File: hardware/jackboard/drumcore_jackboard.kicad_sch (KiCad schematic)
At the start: 11 parts, among them J1 PAD1_TRS_6.35MM, J2 PAD2_TRS_6.35MM, J3 PAD3_TRS_6.35MM, J4 PAD4_TRS_6.35MM, J5 PAD5_TRS_6.35MM, J6 PAD6_TRS_6.35MM, J7 PAD7_TRS_6.35MM, J8 PAD8_TRS_6.35MM, J9 LINK_TO_MAINBOARD, U1 HC4067_CHANNELS, U2 HC4067_CTRL

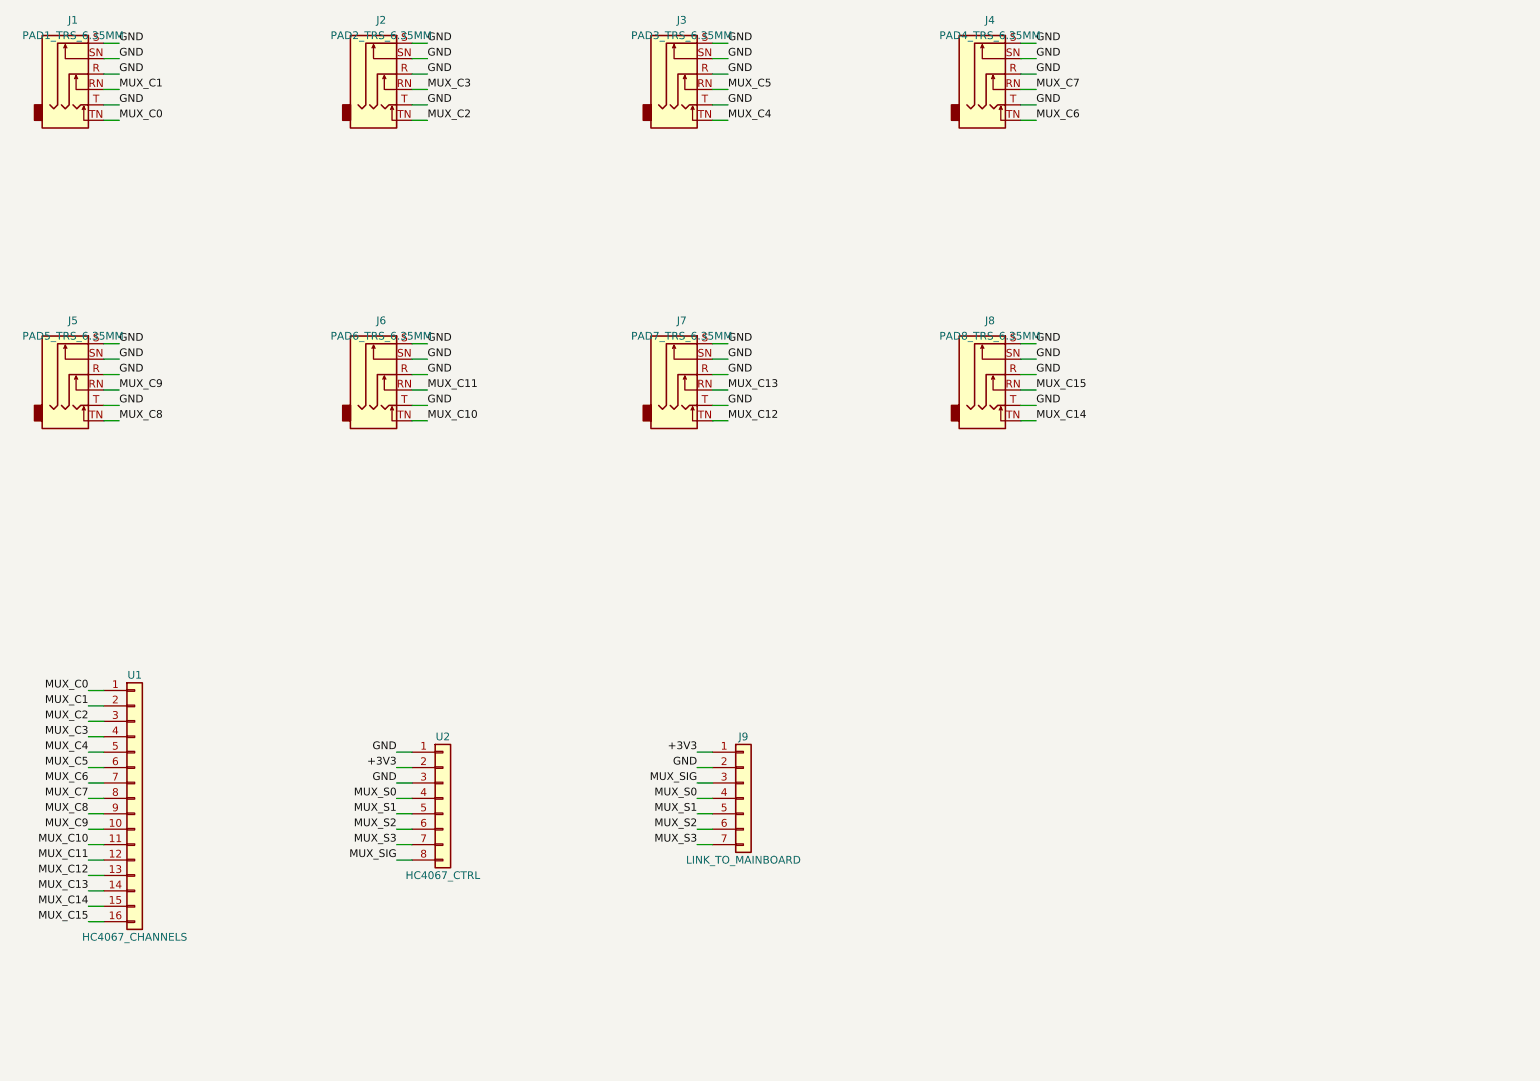
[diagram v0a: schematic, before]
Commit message: Jackboard: pinos T/R corrigidos + rede de protecao por canal; teste do sensor hall
Hardware (hardware/jackboard):
- Esquematico: jacks usavam TN/RN (contato normal/switched) como sinal por
  engano - corrigido pra usar T/R de verdade (Tip=par, Ring=impar), com
  TN/RN/S/SN todos em GND.
- Adicionada rede de protecao por canal (16x): resistor serie 100R + resistor
  paralelo 100k + diodo BAT85, mesma topologia do esquema de referencia da
  HelloDrum-arduino-Library pro MUX (docs/circuit.md).
- PCB: jacks recriados com a netlist corrigida (sync limpo, sem conflito de
  net reatribuido em pad ja roteado) e realinhados no passo fisico de
  22.5mm; os 48 componentes de protecao posicionados no espaco livre entre
  as duas colunas de pads de cada jack; cluster do mux (U1/U2) e do header
  de link (J9) recentralizado sobre a fileira de jacks.

Firmware:
- main.cpp: teste direto do sensor hall (SS49E) do controlador de HH agora
  le so' o GPIO17 (Pad 1 como PAD_SINGLE) - antes lia GPIO17+18 como
  dual-zone, com o segundo canal flutuando sem sensor conectado.
- Novo ambiente isolado [env:test_hall] (src/test_hall.cpp) - mostra a
  leitura bruta do ADC (0-4095) do GPIO17 na tela TFT + Serial, sem
  MUX/encoders/USB-MIDI/BLE/EEPROM, pra validar o sensor isoladamente.

Checkpoint antes de reduzir de 2 pra 1 encoder rotativo na UI - versiona o
estado atual pra poder reverter se a mudanca nao ficar boa.

Co-Authored-By: Claude Sonnet 5 <noreply@anthropic.com>
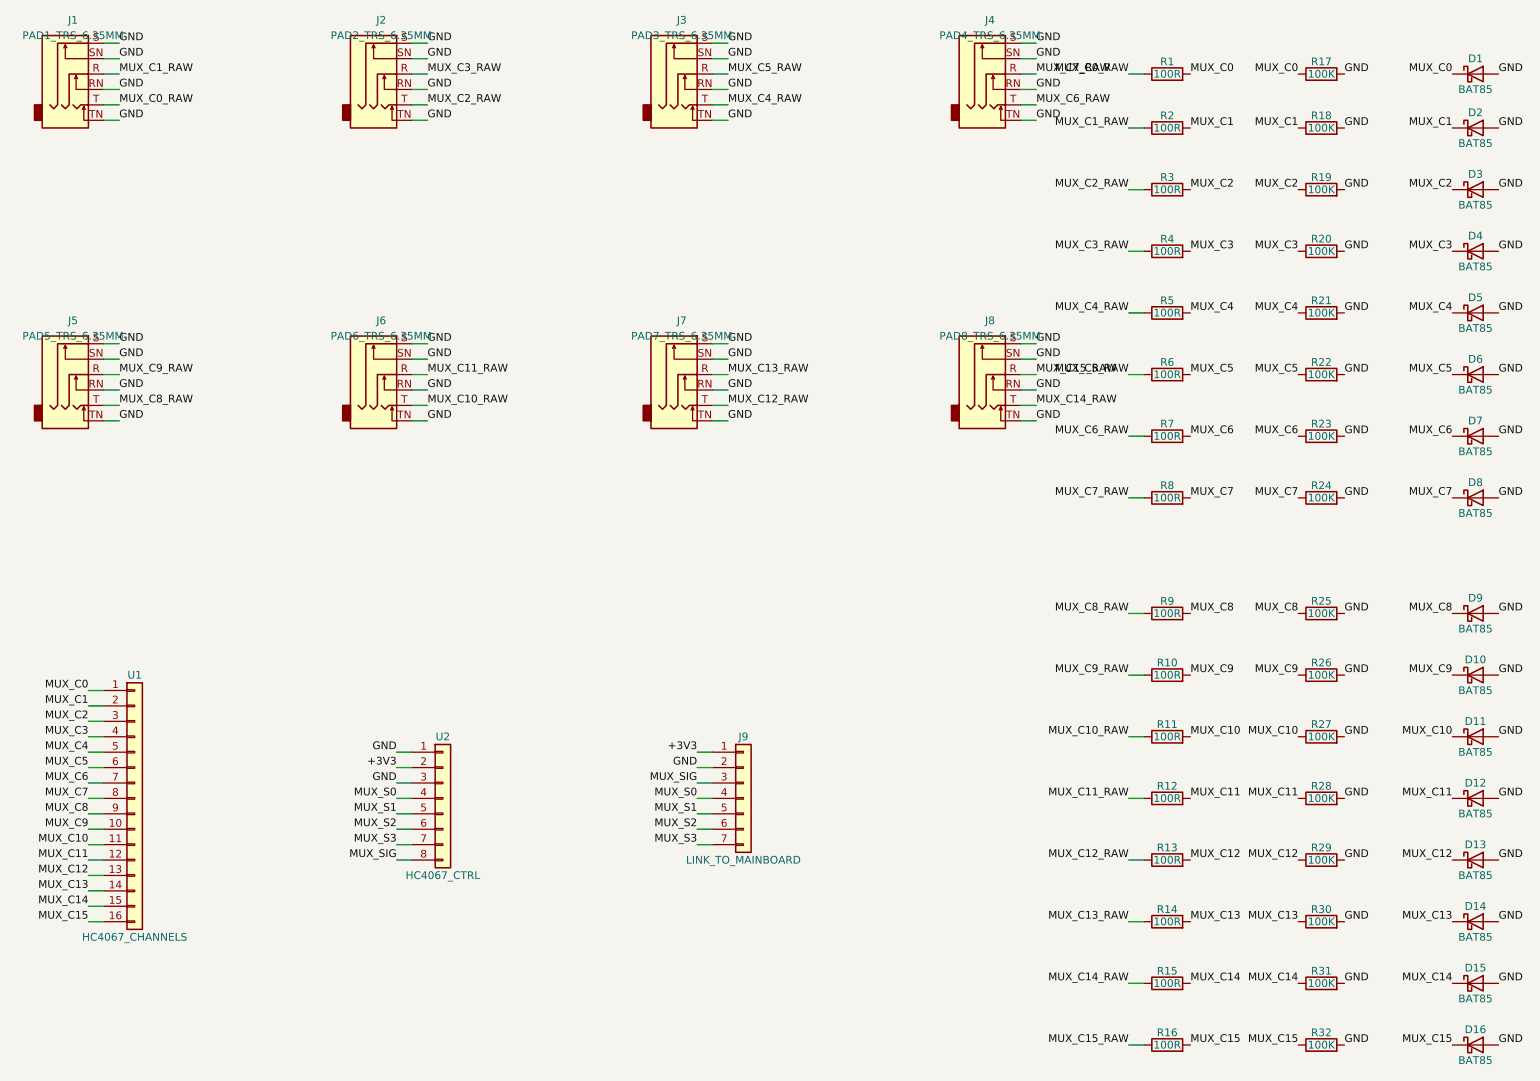
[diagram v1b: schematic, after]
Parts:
- added D1, D10, D11, D12, D13, D14, D15, D16, D2, D3, D4, D5, D6, D7, D8, D9: BAT85, Diode_THT:D_DO-35_SOD27_P7.62mm_Horizontal, symbol Diode:BAT85
- added R1, R10, R11, R12, R13, R14, R15, R16, R2, R3, R4, R5, R6, R7, R8, R9: 100R, Resistor_THT:R_Axial_DIN0207_L6.3mm_D2.5mm_P10.16mm_Horizontal, symbol Device:R
- added R17, R18, R19, R20, R21, R22, R23, R24, R25, R26, R27, R28, R29, R30, R31, R32: 100K, Resistor_THT:R_Axial_DIN0207_L6.3mm_D2.5mm_P10.16mm_Horizontal, symbol Device:R
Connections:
- net GND: now also J1.RN, J1.TN, J2.RN, J2.TN, J3.RN, J3.TN, J4.RN, J4.TN, J5.RN, J5.TN, J6.RN, J6.TN, J7.RN, J7.TN, J8.RN, J8.TN, D1.2 (A), D10.2 (A), D11.2 (A), D12.2 (A), D13.2 (A), D14.2 (A), D15.2 (A), D16.2 (A), D2.2 (A), D3.2 (A), D4.2 (A), D5.2 (A), D6.2 (A), D7.2 (A), D8.2 (A), D9.2 (A), R17.2, R18.2, R19.2, R20.2, R21.2, R22.2, R23.2, R24.2, R25.2, R26.2, R27.2, R28.2, R29.2, R30.2, R31.2, R32.2; no longer J1.R, J1.T, J2.R, J2.T, J3.R, J3.T, J4.R, J4.T, J5.R, J5.T, J6.R, J6.T, J7.R, J7.T, J8.R, J8.T
- net MUX_C0: now also D1.1 (K), R1.2, R17.1; no longer J1.TN
- net MUX_C1: now also D2.1 (K), R18.1, R2.2; no longer J1.RN
- net MUX_C10: now also D11.1 (K), R11.2, R27.1; no longer J6.TN
- net MUX_C11: now also D12.1 (K), R12.2, R28.1; no longer J6.RN
- net MUX_C12: now also D13.1 (K), R13.2, R29.1; no longer J7.TN
- net MUX_C13: now also D14.1 (K), R14.2, R30.1; no longer J7.RN
- net MUX_C14: now also D15.1 (K), R15.2, R31.1; no longer J8.TN
- net MUX_C15: now also D16.1 (K), R16.2, R32.1; no longer J8.RN
- net MUX_C2: now also D3.1 (K), R19.1, R3.2; no longer J2.TN
- net MUX_C3: now also D4.1 (K), R20.1, R4.2; no longer J2.RN
- net MUX_C4: now also D5.1 (K), R21.1, R5.2; no longer J3.TN
- net MUX_C5: now also D6.1 (K), R22.1, R6.2; no longer J3.RN
- net MUX_C6: now also D7.1 (K), R23.1, R7.2; no longer J4.TN
- net MUX_C7: now also D8.1 (K), R24.1, R8.2; no longer J4.RN
- net MUX_C8: now also D9.1 (K), R25.1, R9.2; no longer J5.TN
- net MUX_C9: now also D10.1 (K), R10.2, R26.1; no longer J5.RN
- new net MUX_C0_RAW: J1.T, R1.1
- new net MUX_C10_RAW: J6.T, R11.1
- new net MUX_C11_RAW: J6.R, R12.1
- new net MUX_C12_RAW: J7.T, R13.1
- new net MUX_C13_RAW: J7.R, R14.1
- new net MUX_C14_RAW: J8.T, R15.1
- new net MUX_C15_RAW: J8.R, R16.1
- new net MUX_C1_RAW: J1.R, R2.1
- new net MUX_C2_RAW: J2.T, R3.1
- new net MUX_C3_RAW: J2.R, R4.1
- new net MUX_C4_RAW: J3.T, R5.1
- new net MUX_C5_RAW: J3.R, R6.1
- new net MUX_C6_RAW: J4.T, R7.1
- new net MUX_C7_RAW: J4.R, R8.1
- new net MUX_C8_RAW: J5.T, R9.1
- new net MUX_C9_RAW: J5.R, R10.1
